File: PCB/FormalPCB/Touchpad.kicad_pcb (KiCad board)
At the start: 2 copper layers, 61.2 x 100.1 mm, 5 parts, among them M2 Screw MountingHole_2.2mm_M2

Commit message: PCB Large update & ready for LED debug board
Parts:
- removed the M2 Screw at (72.0, 33.0)
- removed the M2 Screw at (32.0, 16.9)
- removed the REF** at (75.3, 14.6)
- removed the REF** at (22.9, 14.6)
- removed REFFC: Amphenol_F32R-1A7x1-11010_1x10-1MP_P0.5mm_Horizontal, Connector_FFC-FPC:Amphenol_F32R-1A7x1-11010_1x10-1MP_P0.5mm_Horizontal
- added C.1μ: C_0603_1608Metric_Pad1.08x0.95mm_HandSolder, Capacitor_SMD:C_0603_1608Metric_Pad1.08x0.95mm_HandSolder, F.Cu at (29.8, 41.9)
- added C.1μ: C_0603_1608Metric_Pad1.08x0.95mm_HandSolder, Capacitor_SMD:C_0603_1608Metric_Pad1.08x0.95mm_HandSolder, F.Cu at (28.2, 41.9)
- added C1μ: C_0603_1608Metric_Pad1.08x0.95mm_HandSolder, Capacitor_SMD:C_0603_1608Metric_Pad1.08x0.95mm_HandSolder, F.Cu at (31.3, 41.9)
- added C2.2nF: C_0603_1608Metric_Pad1.08x0.95mm_HandSolder, Capacitor_SMD:C_0603_1608Metric_Pad1.08x0.95mm_HandSolder, F.Cu at (27.4, 38.2)
- added CY8CMBR3116: (footprint {dblquote}Package_DFN_QFN:QFN-24-1EP_4x4mm_P0.5m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, Package_DFN_QFN:QFN-24-1EP_4x4mm_P0.5mm_EP2.65x2.65mm_ThermalVias, F.Cu at (32.1, 36.2)
- added M2 Screw: MountingHole_2.2mm_M2, MountingHole:MountingHole_2.2mm_M2, F.Cu at (12.0, 13.0)
- added R4.7k: R_0603_1608Metric_Pad0.98x0.95mm_HandSolder, Resistor_SMD:R_0603_1608Metric_Pad0.98x0.95mm_HandSolder, F.Cu at (31.0, 25.9)
- added R4.7k: R_0603_1608Metric_Pad0.98x0.95mm_HandSolder, Resistor_SMD:R_0603_1608Metric_Pad0.98x0.95mm_HandSolder, F.Cu at (33.8, 25.8)
- added R560: R_0603_1608Metric_Pad0.98x0.95mm_HandSolder, Resistor_SMD:R_0603_1608Metric_Pad0.98x0.95mm_HandSolder, F.Cu at (19.7, 33.2)
- added R560: R_0603_1608Metric_Pad0.98x0.95mm_HandSolder, Resistor_SMD:R_0603_1608Metric_Pad0.98x0.95mm_HandSolder, F.Cu at (19.7, 30.1)
- added R560: R_0603_1608Metric_Pad0.98x0.95mm_HandSolder, Resistor_SMD:R_0603_1608Metric_Pad0.98x0.95mm_HandSolder, F.Cu at (44.4, 33.9)
- added R560: R_0603_1608Metric_Pad0.98x0.95mm_HandSolder, Resistor_SMD:R_0603_1608Metric_Pad0.98x0.95mm_HandSolder, F.Cu at (44.4, 36.9)
- added R560: R_0603_1608Metric_Pad0.98x0.95mm_HandSolder, Resistor_SMD:R_0603_1608Metric_Pad0.98x0.95mm_HandSolder, F.Cu at (44.4, 32.4)
- added R560: R_0603_1608Metric_Pad0.98x0.95mm_HandSolder, Resistor_SMD:R_0603_1608Metric_Pad0.98x0.95mm_HandSolder, F.Cu at (19.7, 31.7)
- added R560: R_0603_1608Metric_Pad0.98x0.95mm_HandSolder, Resistor_SMD:R_0603_1608Metric_Pad0.98x0.95mm_HandSolder, F.Cu at (19.7, 37.8)
- added R560: R_0603_1608Metric_Pad0.98x0.95mm_HandSolder, Resistor_SMD:R_0603_1608Metric_Pad0.98x0.95mm_HandSolder, F.Cu at (44.4, 40.0)
- added R560: R_0603_1608Metric_Pad0.98x0.95mm_HandSolder, Resistor_SMD:R_0603_1608Metric_Pad0.98x0.95mm_HandSolder, F.Cu at (44.4, 41.5)
- added R560: R_0603_1608Metric_Pad0.98x0.95mm_HandSolder, Resistor_SMD:R_0603_1608Metric_Pad0.98x0.95mm_HandSolder, F.Cu at (19.7, 36.2)
- added R560: R_0603_1608Metric_Pad0.98x0.95mm_HandSolder, Resistor_SMD:R_0603_1608Metric_Pad0.98x0.95mm_HandSolder, F.Cu at (19.7, 40.8)
- added R560: R_0603_1608Metric_Pad0.98x0.95mm_HandSolder, Resistor_SMD:R_0603_1608Metric_Pad0.98x0.95mm_HandSolder, F.Cu at (44.4, 30.8)
- added R560: R_0603_1608Metric_Pad0.98x0.95mm_HandSolder, Resistor_SMD:R_0603_1608Metric_Pad0.98x0.95mm_HandSolder, F.Cu at (44.4, 35.4)
- added R560: R_0603_1608Metric_Pad0.98x0.95mm_HandSolder, Resistor_SMD:R_0603_1608Metric_Pad0.98x0.95mm_HandSolder, F.Cu at (44.4, 38.5)
- added R560: R_0603_1608Metric_Pad0.98x0.95mm_HandSolder, Resistor_SMD:R_0603_1608Metric_Pad0.98x0.95mm_HandSolder, F.Cu at (19.7, 34.7)
- added R560: R_0603_1608Metric_Pad0.98x0.95mm_HandSolder, Resistor_SMD:R_0603_1608Metric_Pad0.98x0.95mm_HandSolder, F.Cu at (19.7, 39.3)
- added REF**: PinSocket_1x04_P2.54mm_Vertical, Connector_PinSocket_2.54mm:PinSocket_1x04_P2.54mm_Vertical, F.Cu at (228.3, 9.78)
- added U?: RP2040_Zero, ScottoKeebs_MCU:RP2040_Zero, F.Cu at (11.8, 12.8)
- added debug: PinHeader_1x05_P2.54mm_Vertical, Connector_PinHeader_2.54mm:PinHeader_1x05_P2.54mm_Vertical, F.Cu at (26.9, 10.3)
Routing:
- net TP: track 513.3 -> 212.0 mm, vias 12 -> 0
- net R-CS: track 0.00 -> 218.8 mm
- net GND: track 209.9 -> 68.3 mm, vias 6 -> 3
- net I²C: track 0.00 -> 127.2 mm, vias 0 -> 1
- net VCC: track 0.00 -> 63.3 mm, vias 0 -> 2
- net 595Din: track 0.00 -> 4.93 mm
- net 595latch: track 0.00 -> 4.93 mm
- net 595CLK: track 0.00 -> 4.93 mm
- net CMOD: track 0.00 -> 2.44 mm
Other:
- board size 61.2 x 100.1 mm -> 244 x 150 mm
- board text added: "CS0 CS1 CS2 CS3"
- board text added: "CS15 CS14 CS13 CS12"
- board text added: "CS4 CS5 CS6 CS7"
- board text added: "CS8 CS9 CS10 CS11"
- board text removed: "2.5mm"
- board text removed: "B"
- board text removed: "CS0"
- board text removed: "CS11"
- board text removed: "CS3"
- board text removed: "CS4"
- board text removed: "CS7"
- board text removed: "CS8"

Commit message: Test SPI, regenerate IR code, complete PCB design
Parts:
- added IR: PinHeader_1x09_P2.54mm_Vertical, Connector_PinHeader_2.54mm:PinHeader_1x09_P2.54mm_Vertical, F.Cu at (26.9, 1.78)
- added M2 Screw: MountingHole_2.2mm_M2, MountingHole:MountingHole_2.2mm_M2, F.Cu at (235.0, 25.0)
- added M2 Screw: MountingHole_2.2mm_M2, MountingHole:MountingHole_2.2mm_M2, F.Cu at (220.0, 15.0)
- added M2 Screw: MountingHole_2.2mm_M2, MountingHole:MountingHole_2.2mm_M2, F.Cu at (55.0, 23.0)
- added R220: R_0603_1608Metric_Pad0.98x0.95mm_HandSolder, Resistor_SMD:R_0603_1608Metric_Pad0.98x0.95mm_HandSolder, F.Cu at (236.5, 11.9)
- C.1μ (x2), C1μ: value C_0603_1608Metric_Pad1.08x0.95mm_HandSolder -> C_0402_1005Metric_Pad0.74x0.62mm_HandSolder; footprint Capacitor_SMD:C_0603_1608Metric_Pad1.08x0.95mm_HandSolder -> Capacitor_SMD:C_0402_1005Metric_Pad0.74x0.62mm_HandSolder
- R4.7k (x2): value R_0603_1608Metric_Pad0.98x0.95mm_HandSolder -> C_0402_1005Metric_Pad0.74x0.62mm_HandSolder; footprint Resistor_SMD:R_0603_1608Metric_Pad0.98x0.95mm_HandSolder -> Capacitor_SMD:C_0402_1005Metric_Pad0.74x0.62mm_HandSolder
- SDA SCL VCC GND IRo : renamed from REF**; value PinSocket_1x04_P2.54mm_Vertical -> PinHeader_1x05_P2.54mm_Vertical; footprint Connector_PinSocket_2.54mm:PinSocket_1x04_P2.54mm_Vertical -> Connector_PinHeader_2.54mm:PinHeader_1x05_P2.54mm_Vertical
- moved R560 110.9 mm to (153.9, 20.1), turned to -90 degrees
- moved R560 109.6 mm to (152.4, 20.1), turned to -90 degrees
- moved R560 108.4 mm to (150.9, 20.1), turned to -90 degrees
- moved R560 107.2 mm to (149.4, 20.1), turned to -90 degrees
- moved C.1μ 92.3 mm to (118.1, 21.0)
- moved R4.7k 92.3 mm to (121.3, 7.11)
- moved C.1μ 92.3 mm to (119.6, 21.0)
- moved C1μ 92.3 mm to (121.2, 21.0)
- moved R4.7k 92.2 mm to (124.1, 7.11)
- moved C2.2nF 92.2 mm to (117.2, 17.7)
- moved CY8CMBR3116 92.2 mm to (121.9, 15.7)
- moved R560 92.2 mm to (134.2, 13.5)
- moved R560 92.2 mm to (134.2, 11.9)
- moved R560 92.2 mm to (134.2, 10.4)
- moved R560 92.2 mm to (134.2, 15.0)
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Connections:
- SDA SCL VCC GND IRo  pad 3: GND -> VCC
- SDA SCL VCC GND IRo  pad 4: VCC -> GND
- U? pad 9: (no net) -> IRo
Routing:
- net TP: track 212.0 -> 1246.2 mm, vias 0 -> 32
- net I²C: track 127.2 -> 513.0 mm, vias 1 -> 3
- net IRo: track 0.00 -> 245.5 mm, vias 0 -> 3
- net VCC: track 63.3 -> 296.6 mm, vias 2 -> 3
- net R-CS: track 218.8 -> 369.9 mm
- net GND: track 68.3 -> 17.9 mm, vias 3 -> 4
- net (no net): track 0.00 -> 29.2 mm
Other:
- board size 244 x 150 mm -> 244 x 125 mm
- board text added: "0"
- board text added: "1"
- board text added: "10"
- board text added: "11"
- board text added: "12"
- board text added: "13"
- board text added: "14"
- board text added: "15"
- board text added: "2"
- board text added: "3"
- board text added: "4"
- board text added: "5"
- board text added: "6"
- board text added: "7"
- board text added: "8"
- board text added: "9"
- board text added: "D2 D3 D4 D5 D6 D7 IRo GND VCC"
- board text added: "VCC GND Ltʃ Din CLK"

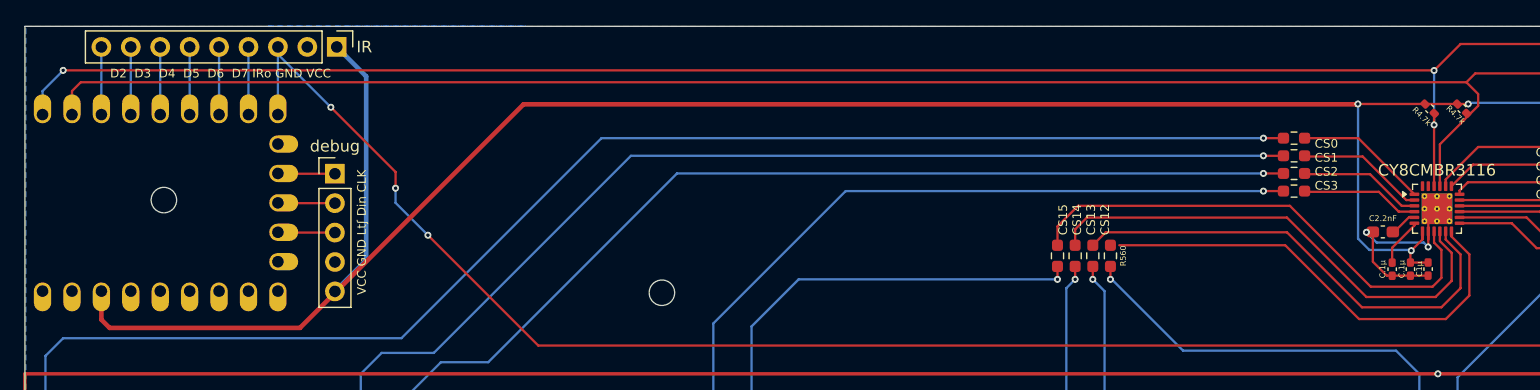
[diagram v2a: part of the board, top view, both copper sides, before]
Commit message: Update complete BOM, edit PCB design, upgrade ConfigCode to PlatformIO
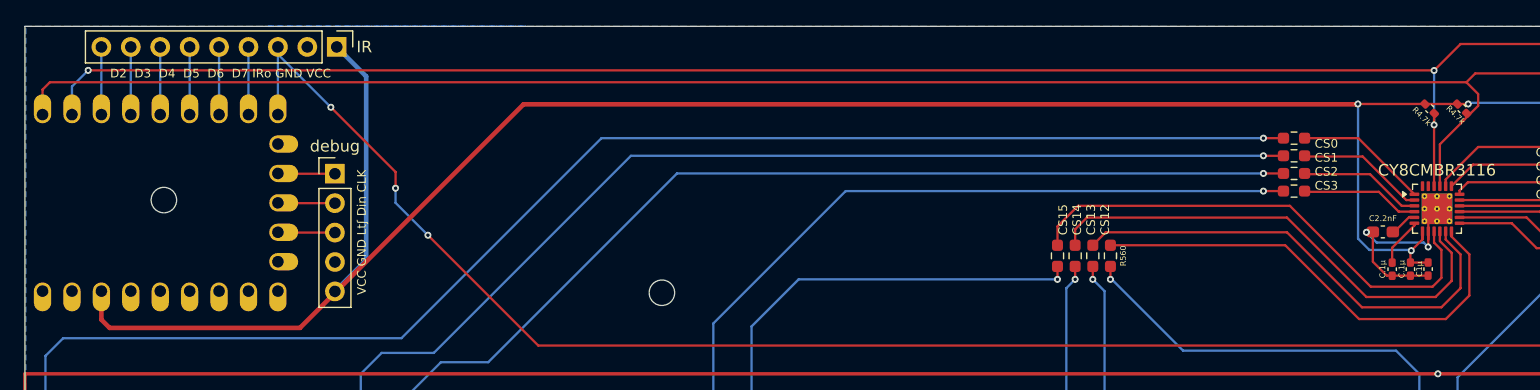
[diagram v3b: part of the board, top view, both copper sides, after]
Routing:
- net R-CS: track 369.9 -> 370.7 mm
